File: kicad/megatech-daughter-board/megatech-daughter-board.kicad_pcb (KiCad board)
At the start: 2 copper layers, 32 parts, among them CN1 Conn_01x07, CN3 Conn_02x20_Counter_Clockwise, IC1 Z084000xP, J1 DB25_Socket

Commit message: Adding back board image into pcb design for alignment
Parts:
- moved C14 222.6 mm to (122.0, -137.9)
- moved C16 222.6 mm to (140.8, -133.2)
- moved CN1 216.7 mm to (151.9, -80.4)
- moved FLT1 216.7 mm to (112.3, -115.1)
- moved FLT2 216.7 mm to (128.2, -114.6)
- moved FLT3 216.7 mm to (144.3, -113.4)
- moved C5 215.3 mm to (100.8, -75.3)
- moved C3 212.8 mm to (31.5, -160.8)
- moved C1 212.8 mm to (-1.45, -127.6)
- moved C10 212.8 mm to (11.8, -156.1)
- moved C11 212.8 mm to (10.6, -138.0)
- moved C12 212.8 mm to (31.3, -156.9)
- moved C13 212.8 mm to (31.3, -138.5)
- moved C2 212.8 mm to (5.76, -127.5)
- moved C4 212.8 mm to (31.1, -144.6)
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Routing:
- net (no net): track 0.00 -> 50.1 mm, vias 77 -> 170
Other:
- board outline added: 150 x 70 mm

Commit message: Further updates to daughter board pcb
All components now placed, but some connections still need to be made
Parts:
- added IC2: NEC D71051C, Package_DIP:DIP-28_W15.24mm, F.Cu at (137.9, 118.0)
- added IC3: HC393, Package_DIP:DIP-14_W7.62mm, F.Cu at (92.0, 77.0)
- added IC4: HC04, Package_DIP:DIP-14_W7.62mm, F.Cu at (92.0, 92.3)
- added IC5: PAL16L8A, Package_DIP:DIP-20_W7.62mm, F.Cu at (162.1, 77.1)
- added IC6: µPD4711C, Package_DIP:DIP-20_W7.62mm, F.Cu at (185.0, 105.1)
- added R1: 1MΩ, Resistor_THT:R_Axial_DIN0204_L3.6mm_D1.6mm_P5.08mm_Horizontal, F.Cu at (76.9, 103.8)
- added R2: 4.7kΩ, Resistor_THT:R_Axial_DIN0204_L3.6mm_D1.6mm_P5.08mm_Horizontal, F.Cu at (76.8, 107.6)
- added R3: 4.7kΩ, Resistor_THT:R_Axial_DIN0204_L3.6mm_D1.6mm_P5.08mm_Horizontal, F.Cu at (98.4, 133.1)
- added X1: 4.9152 MHz, Crystal:Crystal_HC18-U_Horizontal, F.Cu at (84.4, 116.4)
- C3, C4, C7, C8: footprint Capacitor_THT:C_Radial_D8.0mm_H11.5mm_P3.50mm -> Capacitor_THT:CP_Radial_D5.0mm_P2.50mm
- C5, C6, C9: footprint Capacitor_THT:C_Radial_D10.0mm_H16.0mm_P5.00mm -> Capacitor_THT:CP_Radial_D10.0mm_P5.00mm
- CN1: value Conn_01x07 -> JST NH 7P
- FLT1, FLT10, FLT11, FLT12, FLT2, FLT3, FLT4, FLT5, FLT6, FLT7, FLT8, FLT9: footprint Filter:Filter_KEMET_PZB300_24.0x12.5mm_P10.0mm -> Crystal:Resonator-3Pin_W6.0mm_H3.0mm
- moved C14 271.9 mm to (143.1, 133.1), turned to 90 degrees
- moved C10 257.4 mm to (92.0, 88.4), turned to 180 degrees
- moved C11 255.1 mm to (92.0, 103.8), turned to 180 degrees
- moved C1 251.6 mm to (76.9, 111.5)
- moved C16 250.8 mm to (162.1, 116.7)
- moved C2 250.5 mm to (80.7, 111.5)
- moved C4 249.9 mm to (98.2, 96.1)
- moved C3 249.4 mm to (98.4, 79.5)
- moved C12 249.4 mm to (98.3, 83.3)
- moved C13 247.9 mm to (98.3, 100.2)
- moved FLT1 245.7 mm to (162.1, 125.5), turned to 90 degrees
- moved FLT2 243.2 mm to (167.2, 125.5), turned to 90 degrees
- moved FLT3 240.5 mm to (172.3, 125.5), turned to 90 degrees
- moved FLT7 240.2 mm to (194.2, 76.9)
- moved FLT8 239.1 mm to (199.2, 87.2), turned to 90 degrees
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- renumbered J1 to CN2
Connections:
- net Net-(CN3-Pin_1) renamed /ZA11
- net Net-(CN3-Pin_10) renamed /ZD6
- net Net-(CN3-Pin_12) renamed /ZD2
- net Net-(CN3-Pin_13) renamed /ZD7
- net Net-(CN3-Pin_14) renamed /ZD0
- net Net-(CN3-Pin_15) renamed /ZD1
- net Net-(CN3-Pin_2) renamed /ZA12
- net Net-(CN3-Pin_3) renamed /ZA13
- net Net-(CN3-Pin_39) renamed /ZA9
- net Net-(CN3-Pin_4) renamed /ZA14
- net Net-(CN3-Pin_40) renamed /ZA10
- net Net-(CN3-Pin_5) renamed /ZA15
- net Net-(CN3-Pin_7) renamed /ZD4
- net Net-(CN3-Pin_8) renamed /ZD3
- net Net-(CN3-Pin_9) renamed /ZD5
- C1 pad 1: unconnected-(C1-Pad1) -> Net-(C1-Pad1)
- C1 pad 2: unconnected-(C1-Pad2) -> GND
- C10 pad 1: unconnected-(C10-Pad1) -> VCC
- C10 pad 2: unconnected-(C10-Pad2) -> GND
- C11 pad 1: unconnected-(C11-Pad1) -> VCC
- C11 pad 2: unconnected-(C11-Pad2) -> GND
- C12 pad 1: unconnected-(C12-Pad1) -> VCC
- C12 pad 2: unconnected-(C12-Pad2) -> GND
- C13 pad 1: unconnected-(C13-Pad1) -> VCC
- C13 pad 2: unconnected-(C13-Pad2) -> GND
- C14 pad 1: unconnected-(C14-Pad1) -> VCC
- C14 pad 2: unconnected-(C14-Pad2) -> GND
- C15 pad 1: unconnected-(C15-Pad1) -> VCC
- C15 pad 2: unconnected-(C15-Pad2) -> GND
- C16 pad 1: unconnected-(C16-Pad1) -> VCC
- C16 pad 2: unconnected-(C16-Pad2) -> GND
- C2 pad 1: unconnected-(C2-Pad1) -> Net-(IC4-Pin_9)
- C2 pad 2: unconnected-(C2-Pad2) -> GND
- C3 pad 1: unconnected-(C3-Pad1) -> VCC
- C4 pad 1: unconnected-(C4-Pad1) -> VCC
- C4 pad 2: unconnected-(C4-Pad2) -> GND
- C5 pad 1: unconnected-(C5-Pad1) -> VCC
- C5 pad 2: unconnected-(C5-Pad2) -> GND
- C6 pad 1: unconnected-(C6-Pad1) -> GND
- C6 pad 2: unconnected-(C6-Pad2) -> -12V_FILT
- C7 pad 1: unconnected-(C7-Pad1) -> +12V_FILT
- C7 pad 2: unconnected-(C7-Pad2) -> VCC
- C8 pad 2: unconnected-(C8-Pad2) -> -12V_FILT
- C9 pad 1: unconnected-(C9-Pad1) -> +12V_FILT
- CN1 pad 1: unconnected-(CN1-Pin_1-Pad1) -> +12V
- CN1 pad 2: unconnected-(CN1-Pin_2-Pad2) -> -12V
- CN1 pad 3: unconnected-(CN1-Pin_3-Pad3) -> GND
- CN1 pad 4: unconnected-(CN1-Pin_4-Pad4) -> GND
- CN1 pad 5: unconnected-(CN1-Pin_5-Pad5) -> GND
- CN1 pad 6: unconnected-(CN1-Pin_6-Pad6) -> +5V
- CN2 pad 18: unconnected-(J1-P18-Pad18) -> VCC_FILT
- CN3 pad 11: unconnected-(CN3-Pin_11-Pad11) -> VCC
- CN3 pad 16: unconnected-(CN3-Pin_16-Pad16) -> /!ZINT
- CN3 pad 17: unconnected-(CN3-Pin_17-Pad17) -> /!ZNMI
- CN3 pad 18: unconnected-(CN3-Pin_18-Pad18) -> /!ZHALT
- CN3 pad 19: unconnected-(CN3-Pin_19-Pad19) -> /!ZMREQ
- CN3 pad 20: unconnected-(CN3-Pin_20-Pad20) -> /!ZIOREQ
- CN3 pad 21: unconnected-(CN3-Pin_21-Pad21) -> /!ZRD
- CN3 pad 22: unconnected-(CN3-Pin_22-Pad22) -> /!ZWR
- CN3 pad 23: unconnected-(CN3-Pin_23-Pad23) -> /!ZBUSACK
- CN3 pad 24: unconnected-(CN3-Pin_24-Pad24) -> /!ZWAIT
- CN3 pad 25: unconnected-(CN3-Pin_25-Pad25) -> /!ZBUSRQ
- CN3 pad 26: unconnected-(CN3-Pin_26-Pad26) -> /!RESET
- CN3 pad 27: unconnected-(CN3-Pin_27-Pad27) -> /!ZM1
- CN3 pad 28: unconnected-(CN3-Pin_28-Pad28) -> /!OE
- CN3 pad 29: unconnected-(CN3-Pin_29-Pad29) -> GND
- CN3 pad 30: unconnected-(CN3-Pin_30-Pad30) -> /ZA0
- CN3 pad 31: unconnected-(CN3-Pin_31-Pad31) -> /ZA1
- CN3 pad 32: unconnected-(CN3-Pin_32-Pad32) -> /ZA2
- CN3 pad 33: unconnected-(CN3-Pin_33-Pad33) -> /ZA3
- CN3 pad 34: unconnected-(CN3-Pin_34-Pad34) -> /ZA4
- CN3 pad 35: unconnected-(CN3-Pin_35-Pad35) -> /ZA5
- CN3 pad 36: unconnected-(CN3-Pin_36-Pad36) -> /ZA6
- CN3 pad 37: unconnected-(CN3-Pin_37-Pad37) -> /ZA7
- CN3 pad 38: unconnected-(CN3-Pin_38-Pad38) -> /ZA8
- CN3 pad 6: unconnected-(CN3-Pin_6-Pad6) -> /ZCLK
- FLT1 pad 1: unconnected-(FLT1-Pad1) -> +5V
- FLT1 pad 2: unconnected-(FLT1-Pad2) -> GND
- FLT1 pad 3: unconnected-(FLT1-Pad3) -> VCC
- FLT12 pad 1: unconnected-(FLT12-Pad1) -> +12V_FILT
- FLT2 pad 1: unconnected-(FLT2-Pad1) -> GND
- FLT2 pad 3: unconnected-(FLT2-Pad3) -> GND
- FLT3 pad 1: unconnected-(FLT3-Pad1) -> GND
- FLT3 pad 3: unconnected-(FLT3-Pad3) -> GND
- FLT4 pad 1: unconnected-(FLT4-Pad1) -> GND
- FLT4 pad 3: unconnected-(FLT4-Pad3) -> GND
- FLT5 pad 1: unconnected-(FLT5-Pad1) -> -12V
- FLT5 pad 2: unconnected-(FLT5-Pad2) -> GND
- FLT5 pad 3: unconnected-(FLT5-Pad3) -> -12V_FILT
- FLT6 pad 1: unconnected-(FLT6-Pad1) -> +12V
- FLT6 pad 2: unconnected-(FLT6-Pad2) -> GND
- FLT6 pad 3: unconnected-(FLT6-Pad3) -> +12V_FILT
- FLT7 pad 1: unconnected-(FLT7-Pad1) -> VCC
- FLT7 pad 3: unconnected-(FLT7-Pad3) -> VCC_FILT
- IC1 pad 11: unconnected-(IC1-V_{CC}-Pad11) -> VCC
- IC1 pad 16: unconnected-(IC1-~{INT}-Pad16) -> /!ZINT
- IC1 pad 17: unconnected-(IC1-~{NMI}-Pad17) -> /!ZNMI
- IC1 pad 18: unconnected-(IC1-~{HALT}-Pad18) -> /!ZHALT
- IC1 pad 19: unconnected-(IC1-~{MREQ}-Pad19) -> /!ZMREQ
- IC1 pad 20: unconnected-(IC1-~{IORQ}-Pad20) -> /!ZIOREQ
- IC1 pad 21: unconnected-(IC1-~{RD}-Pad21) -> /!ZRD
- IC1 pad 22: unconnected-(IC1-~{WR}-Pad22) -> /!ZWR
- IC1 pad 23: unconnected-(IC1-~{BUSACK}-Pad23) -> /!ZBUSACK
- IC1 pad 24: unconnected-(IC1-~{WAIT}-Pad24) -> /!ZWAIT
- IC1 pad 25: unconnected-(IC1-~{BUSREQ}-Pad25) -> /!ZBUSRQ
- IC1 pad 26: unconnected-(IC1-~{RESET}-Pad26) -> /!RESET
- IC1 pad 27: unconnected-(IC1-~{M1}-Pad27) -> /!ZM1
- IC1 pad 28: unconnected-(IC1-~{RFSH}-Pad28) -> /!OE
- IC1 pad 29: unconnected-(IC1-GND-Pad29) -> GND
- IC1 pad 30: unconnected-(IC1-A_{0}-Pad30) -> /ZA0
- IC1 pad 31: unconnected-(IC1-A_{1}-Pad31) -> /ZA1
- IC1 pad 32: unconnected-(IC1-A_{2}-Pad32) -> /ZA2
- IC1 pad 33: unconnected-(IC1-A_{3}-Pad33) -> /ZA3
- IC1 pad 34: unconnected-(IC1-A_{4}-Pad34) -> /ZA4
- IC1 pad 35: unconnected-(IC1-A_{5}-Pad35) -> /ZA5
- IC1 pad 36: unconnected-(IC1-A_{6}-Pad36) -> /ZA6
- IC1 pad 37: unconnected-(IC1-A_{7}-Pad37) -> /ZA7
- IC1 pad 38: unconnected-(IC1-A_{8}-Pad38) -> /ZA8
- IC1 pad 6: unconnected-(IC1-CLK-Pad6) -> /ZCLK
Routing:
- net /!RESET: track 0.00 -> 115.1 mm, vias 0 -> 2
- net /ZD0: track 0.00 -> 93.2 mm, vias 0 -> 1
- net unconnected-(IC2-Pin_14-Pad14): track 0.00 -> 89.8 mm, vias 0 -> 2
- net unconnected-(IC2-Pin_13-Pad13): track 0.00 -> 89.6 mm, vias 0 -> 2
- net /!ZMREQ: track 0.00 -> 88.6 mm, vias 0 -> 1
- net /!ZNMI: track 0.00 -> 73.3 mm, vias 0 -> 1
- net /!ZRD: track 0.00 -> 71.3 mm, vias 0 -> 1
- net /!ZWR: track 0.00 -> 68.2 mm, vias 0 -> 1
- net /ZCLK: track 0.00 -> 63.4 mm, vias 0 -> 1
- net /ZD2: track 0.00 -> 58.9 mm, vias 0 -> 2
- net /!OE: track 0.00 -> 58.1 mm, vias 0 -> 1
- net GND: track 0.00 -> 56.5 mm, vias 0 -> 7
- net /ZA0: track 0.00 -> 55.3 mm, vias 0 -> 1
- net unconnected-(IC2-Pin_9-Pad9): track 0.00 -> 52.1 mm, vias 0 -> 5
- net /ZD4: track 0.00 -> 49.5 mm, vias 0 -> 1
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- added copper zone on B.Cu, net (none)
- added copper zone on B.Cu, net +12V
- added copper zone on B.Cu, net +12V_FILT
- added copper zone on B.Cu, net +5V
- added copper zone on B.Cu, net -12V
- added copper zone on B.Cu, net -12V_FILT
- added copper zone on B.Cu, net GND
- added copper zone on B.Cu, net VCC
- added copper zone on B.Cu, net VCC_FILT
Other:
- outline, holes or cut-outs redrawn
- board text added: "837-6972"

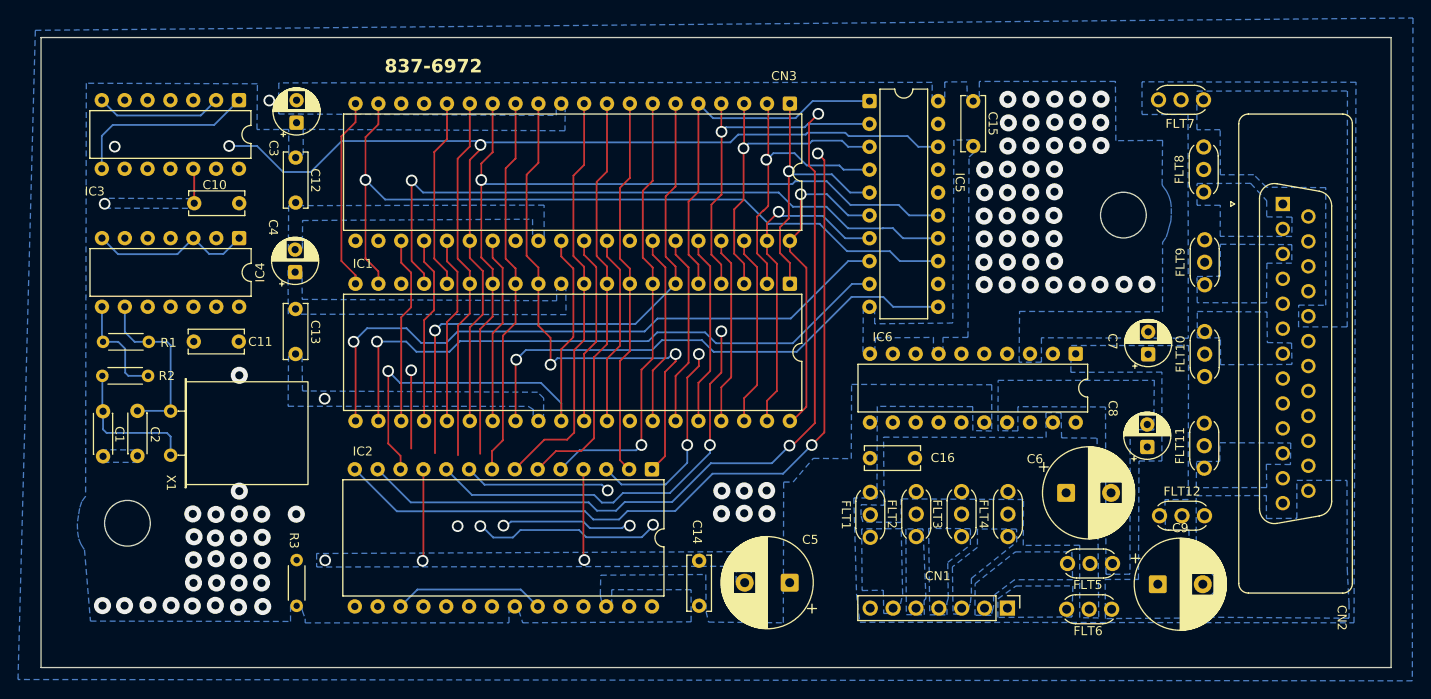
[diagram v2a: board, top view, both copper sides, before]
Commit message: Further updates to the daughterboard pcb
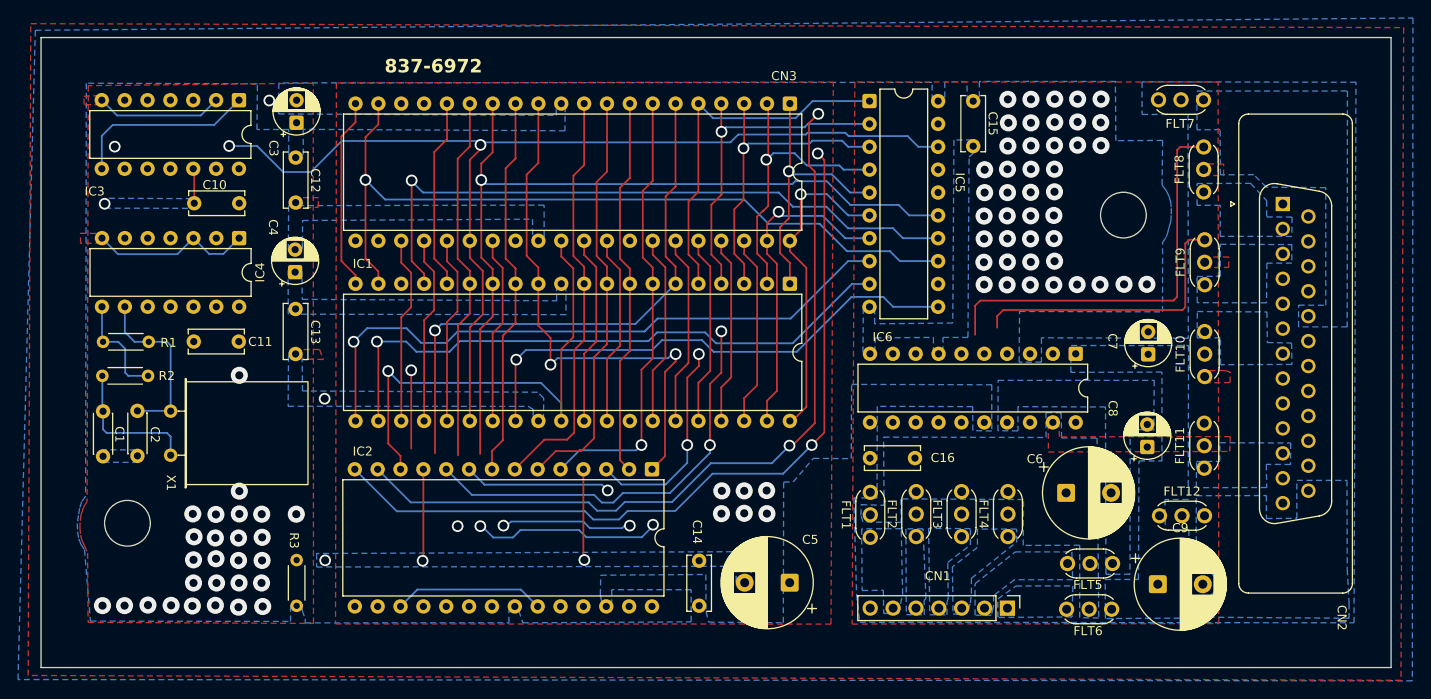
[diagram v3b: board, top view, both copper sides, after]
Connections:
- C8 pad 1: unconnected-(C8-Pad1) -> GND
- CN2 pad 11: unconnected-(CN2-Pad11) -> Net-(CN2-Pad11)
- CN2 pad 2: unconnected-(CN2-Pad2) -> Net-(CN2-Pad2)
- CN2 pad 25: unconnected-(CN2-P25-Pad25) -> Net-(CN2-P25)
- CN2 pad 3: unconnected-(CN2-Pad3) -> Net-(CN2-Pad3)
- CN2 pad 7: unconnected-(CN2-Pad7) -> Net-(CN2-Pad7)
- FLT10 pad 1: unconnected-(FLT10-Pad1) -> GND
- FLT10 pad 3: unconnected-(FLT10-Pad3) -> Net-(CN2-Pad7)
- FLT11 pad 1: unconnected-(FLT11-Pad1) -> Net-(CN2-Pad11)
- FLT11 pad 2: unconnected-(FLT11-Pad2) -> GND
- FLT12 pad 3: unconnected-(FLT12-Pad3) -> Net-(CN2-P25)
- FLT8 pad 1: unconnected-(FLT8-Pad1) -> Net-(CN2-Pad2)
- FLT8 pad 2: unconnected-(FLT8-Pad2) -> GND
- FLT9 pad 1: unconnected-(FLT9-Pad1) -> Net-(CN2-Pad3)
- FLT9 pad 2: unconnected-(FLT9-Pad2) -> GND
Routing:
- net unconnected-(FLT8-Pad3): track 0.00 -> 45.5 mm
- net unconnected-(FLT9-Pad3): track 0.00 -> 32.0 mm
- added copper zone on F.Cu, net GND
- added copper zone on B.Cu, net Net-(CN2-P25)
- added copper zone on B.Cu, net Net-(CN2-Pad11)
- added copper zone on B.Cu, net Net-(CN2-Pad2)
- added copper zone on B.Cu, net Net-(CN2-Pad3)
- added copper zone on B.Cu, net Net-(CN2-Pad7)
- removed copper zone on B.Cu, net (none)

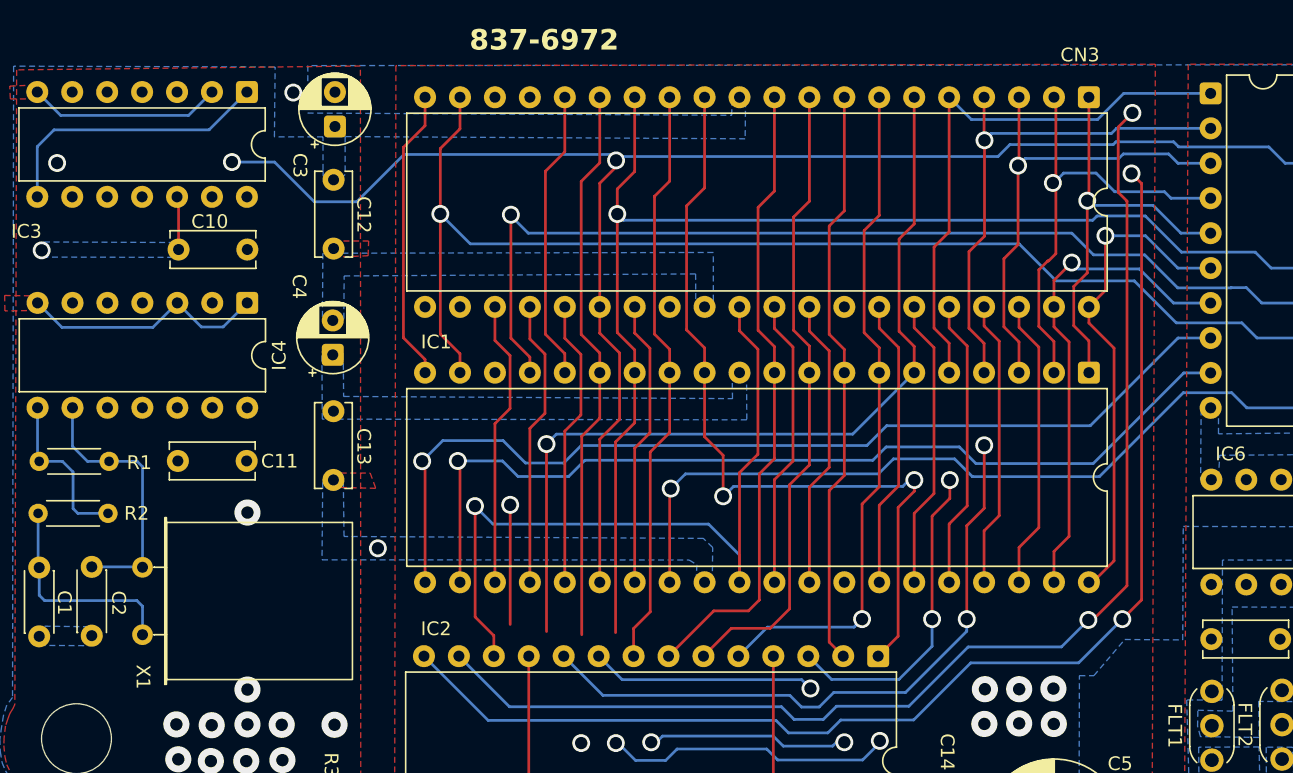
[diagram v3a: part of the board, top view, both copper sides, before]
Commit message: Further improvements to daughter board pcb
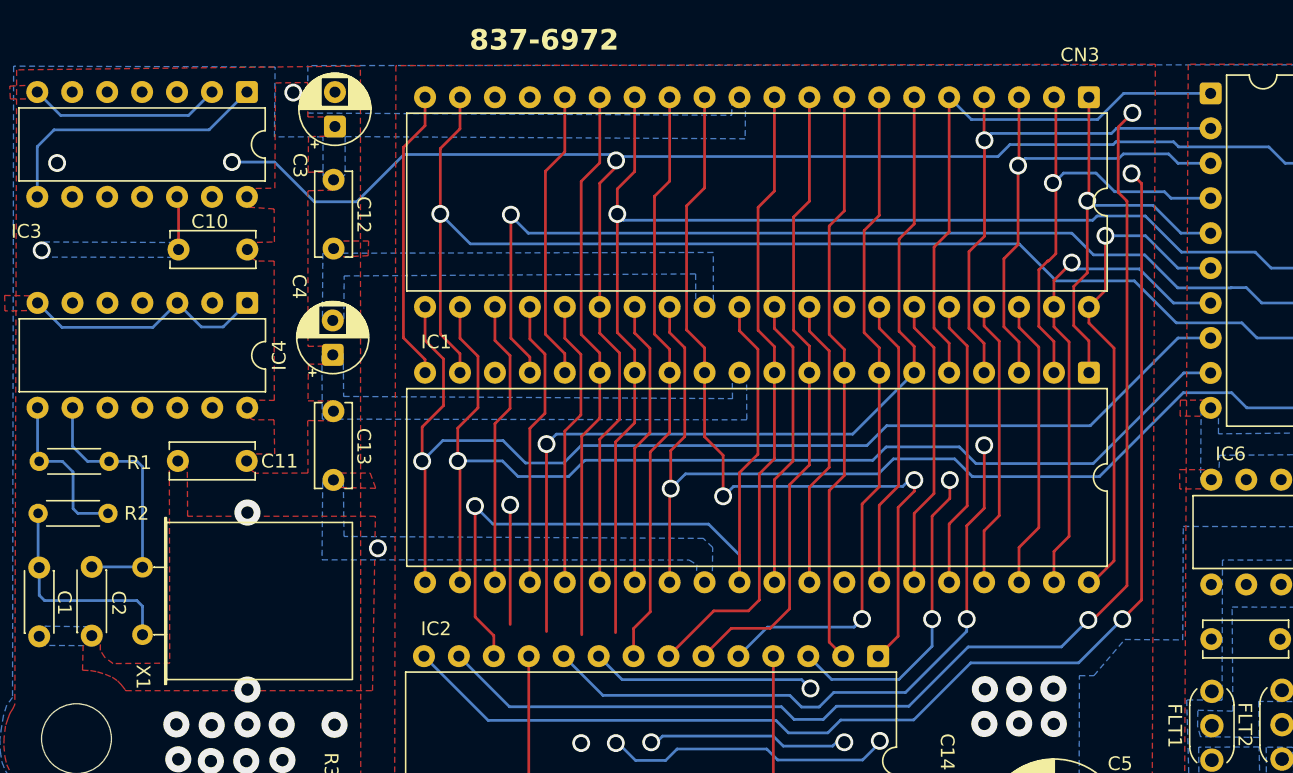
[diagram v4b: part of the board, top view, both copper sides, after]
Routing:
- net /!OE: track 58.1 -> 72.2 mm
- net /!ZRD: track 71.3 -> 83.7 mm
- net /!ZWR: track 68.2 -> 80.6 mm
- added copper zone on F.Cu, net VCC
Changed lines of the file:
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@@
 	)
 	(segment
+		(start 106.28 96.36)
+		(end 106.28 99.76)
+		(width 0.2)
+		(layer "F.Cu")
+		(net "/!ZRD")
+	)
+	(segment
+		(start 104.94 92.58)
+		(end 104.94 95.02)
+		(width 0.2)
+		(layer "F.Cu")
+		(net "/!ZRD")
+	)
+	(segment
+		(start 104.73 101.31)
+		(end 104.73 103.8)
+		(width 0.2)
+		(layer "F.Cu")
+		(net "/!ZRD")
+	)
+	(segment
+		(start 104.94 95.02)
+		(end 106.28 96.36)
+		(width 0.2)
+		(layer "F.Cu")
+		(net "/!ZRD")
+	)
+	(segment
 		(start 104.94 104.01)
 		(end 104.73 103.8)
@@
 		(net "/!ZRD")
 	)
+	(segment
+		(start 106.28 99.76)
+		(end 104.73 101.31)
+		(width 0.2)
+		(layer "F.Cu")
+		(net "/!ZRD")
+	)
 	(via
 		(at 104.73 103.8)
@@
 	)
 	(segment
+		(start 108.79 96.17)
+		(end 108.79 99.92)
+		(width 0.2)
+		(layer "F.Cu")
+		(net "/!ZWR")
+	)
+	(segment
+		(start 107.48 92.58)
+		(end 107.48 94.86)
+		(width 0.2)
+		(layer "F.Cu")
+		(net "/!ZWR")
+	)
+	(segment
+		(start 107.32 101.39)
+		(end 107.32 103.78)
+		(width 0.2)
+		(layer "F.Cu")
+		(net "/!ZWR")
+	)
+	(segment
+		(start 107.48 94.86)
+		(end 108.79 96.17)
+		(width 0.2)
+		(layer "F.Cu")
+		(net "/!ZWR")
+	)
+	(segment
 		(start 107.48 112.6)
 		(end 107.48 103.94)
@@
 		(net "/!ZWR")
 	)
+	(segment
+		(start 108.79 99.92)
+		(end 107.32 101.39)
+		(width 0.2)
+		(layer "F.Cu")
+		(net "/!ZWR")
+	)
 	(via
 		(at 107.32 103.78)
@@
 	)
 	(segment
+		(start 123.82 95.55)
+		(end 123.82 102.01)
+		(width 0.2)
+		(layer "F.Cu")
+		(net "/!OE")
+	)
+	(segment
+		(start 123.82 102.01)
+		(end 122.8 103.03)
+		(width 0.2)
+		(layer "F.Cu")
+		(net "/!OE")
+	)
+	(segment
+		(start 122.72 92.58)
+		(end 122.72 94.45)
+		(width 0.2)
+		(layer "F.Cu")
+		(net "/!OE")
+	)
+	(segment
+		(start 122.72 94.45)
+		(end 123.82 95.55)
+		(width 0.2)
+		(layer "F.Cu")
+		(net "/!OE")
+	)
+	(segment
 		(start 122.72 105.87)
 		(end 122.72 112.6)
@@
 		(net "/!OE")
 	)
+	(segment
+		(start 122.8 103.03)
+		(end 122.8 105.79)
+		(width 0.2)
+		(layer "F.Cu")
+		(net "/!OE")
+	)
 	(via
 		(at 122.8 105.79)
@@
 		(layer "F.Cu")
 		(hatch edge 0.5)
+		(priority 34)
+		(connect_pads yes
+			(clearance 0.5)
+		)
+		(min_thickness 0.25)
+		(fill yes
+			(thermal_gap 0.5)
+			(thermal_bridge_width 0.5)
+			(island_removal_mode 0)
+		)
+		(polygon
+			(pts
+				(xy 101.33 107.8) (xy 87.68 107.8) (xy 87.65 103.74) (xy 86.35 103.77) (xy 86.38 118.48) (xy 82.26 118.51)
+				(xy 81.66 118.06) (xy 81.33 117.55) (xy 81.33 116.32) (xy 80.1 116.47) (xy 80.04 118.99) (xy 80.61 119.02)
+				(xy 81.12 119.11) (xy 81.69 119.29) (xy 82.2 119.5) (xy 82.59 119.77) (xy 82.86 120.05) (xy 83.14 120.41)
+				(xy 83.18 120.48) (xy 101.12 120.48)
+			)
+		)
+	)
+	(zone
+		(net "VCC")
+		(layer "F.Cu")
+		(hatch edge 0.5)
+		(priority 33)
+		(connect_pads yes
+			(clearance 0.5)
+		)
+		(min_thickness 0.25)
+		(fill yes
+			(thermal_gap 0.5)
+			(thermal_bridge_width 0.5)
+			(island_removal_mode 0)
+		)
+		(polygon
+			(pts
+				(xy 96.36 104.66) (xy 92.62 104.67) (xy 91.97 104.22) (xy 91.97 103.26) (xy 94.01 103.28) (xy 93.96 100.79)
+				(xy 92.43 100.79) (xy 91.8 100.41) (xy 92.19 99.35) (xy 93.98 99.38) (xy 93.97 89.25) (xy 92.7 89.25)
+				(xy 92.02 88.84) (xy 92.02 87.91) (xy 93.99 87.86) (xy 93.97 85.46) (xy 91.98 85.32) (xy 91.93 83.98)
+				(xy 94.02 83.95) (xy 94.07 76.3) (xy 96.4 76.27) (xy 96.42 78.77) (xy 98.23 78.77) (xy 98.39 80.16)
+				(xy 96.47 80.2) (xy 96.44 82.79) (xy 98.39 82.77) (xy 98.27 84.09) (xy 96.42 84.14) (xy 96.43 95.45)
+				(xy 98.18 95.42) (xy 98.28 96.74) (xy 96.46 96.74) (xy 96.43 99.41) (xy 98.27 99.43) (xy 98.28 100.87)
+				(xy 96.41 100.84) (xy 96.43 104.66)
+			)
+		)
+	)
+	(zone
+		(net "GND")
+		(layer "F.Cu")
+		(hatch edge 0.5)
+		(priority 32)
+		(connect_pads yes
+			(clearance 0.5)
+		)
+		(min_thickness 0.25)
+		(fill yes
+			(thermal_gap 0.5)
+			(thermal_bridge_width 0.5)
+			(island_removal_mode 0)
+		)
+		(polygon
+			(pts
+				(xy 159.79 104.41) (xy 162.04 104.42) (xy 162.06 105.8) (xy 159.81 105.82)
+			)
+		)
+	)
+	(zone
+		(net "GND")
+		(layer "F.Cu")
+		(hatch edge 0.5)
 		(priority 25)
 		(connect_pads yes
@@
 			)
 		)
+	)
+	(zone
+		(net "GND")
+		(layer "F.Cu")
+		(hatch edge 0.5)
+		(priority 31)
+		(connect_pads yes
+			(clearance 0.5)
+		)
+		(min_thickness 0.25)
+		(fill yes
+			(thermal_gap 0.5)
+			(thermal_bridge_width 0.5)
+			(island_removal_mode 0)
+		)
+		(polygon
+			(pts
+				(xy 159.85 99.36) (xy 161.99 99.36) (xy 162 100.53) (xy 159.83 100.52)
+			)
+		)
